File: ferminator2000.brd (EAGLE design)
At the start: 111.2 x 58 mm, 120 parts, among them CN1 MINIB, IC1 FT232RL, IC2 REF01D, Q1 STP5NA50, Q2 STP5NA50, SW1 ENCODER_SW1-PEC12, U1 DSPIC33FJ256GP510A

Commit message: added pin definitions
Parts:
- C1: value (none) -> 100u
- C14, C19, C20: value (none) -> 10u
- R10, R11, R12, R13, R8, R9: value 47k -> 10k
- R16: value 1k -> 22
- R2, R3: value 1K -> 1k
- R25, R26, R27, R28, R29, R30, R31, R32: value 1k -> 2.7k
- R4, R6: value 1k -> 5.6k
- R41, R42: value (none) -> 10k
- renumbered U$2 to U2

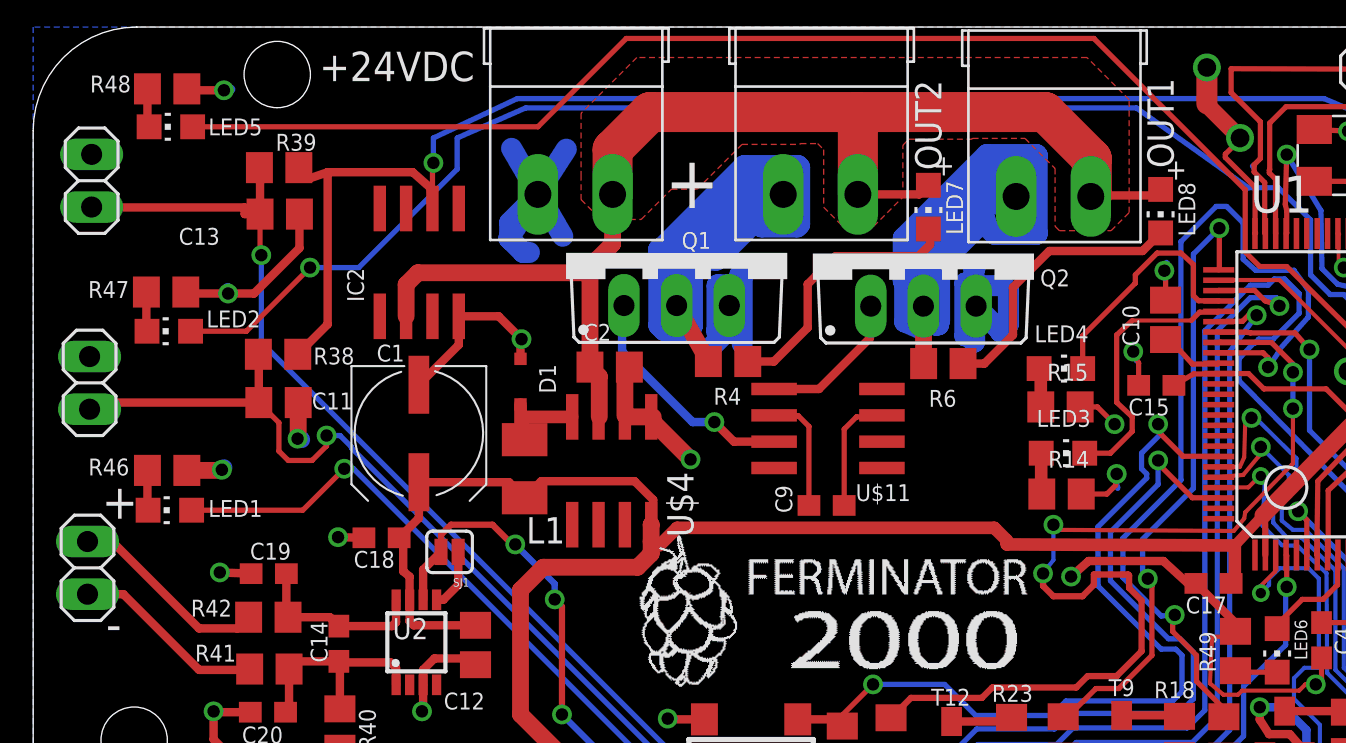
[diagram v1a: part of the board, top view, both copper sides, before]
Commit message: Added Control Lines for FETs
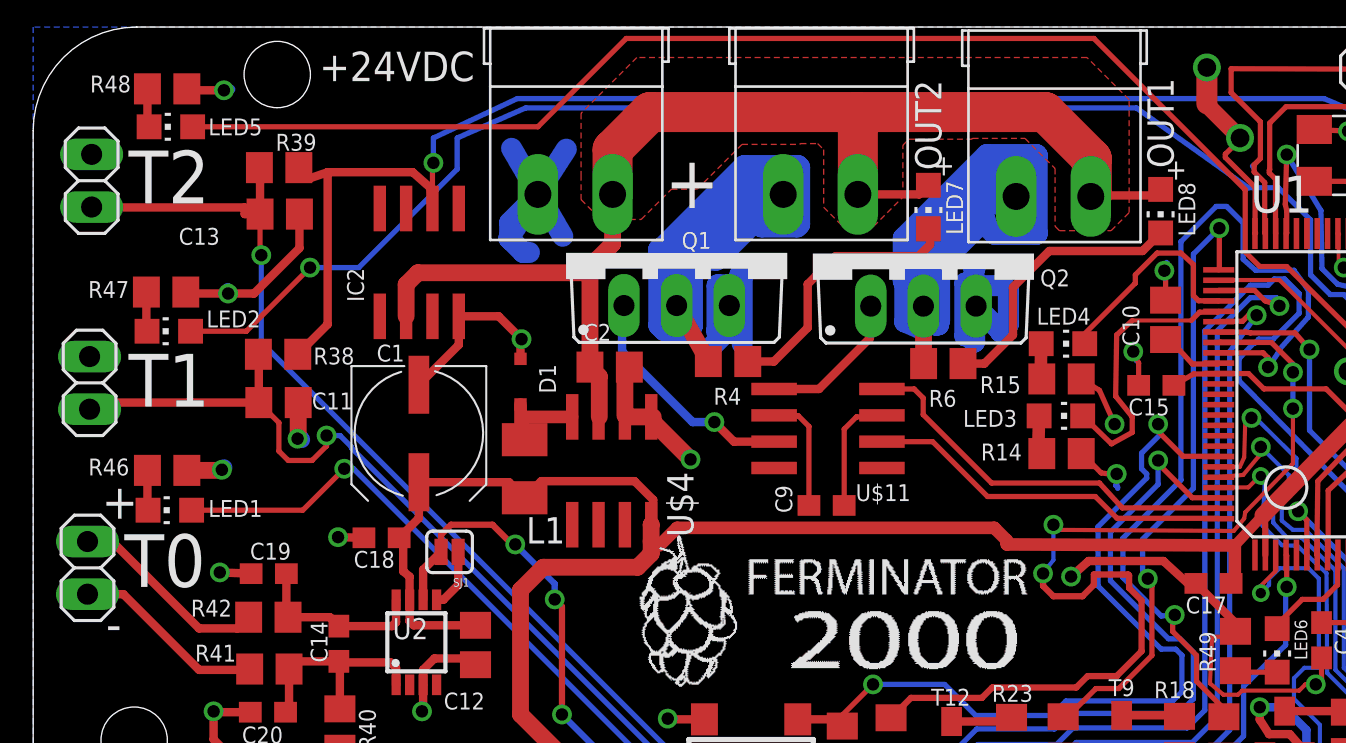
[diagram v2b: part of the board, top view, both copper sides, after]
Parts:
- moved R14 1.95 mm to (51.3, 38.0)
- moved LED3 1.80 mm to (51.2, 39.8)
- moved R15 1.35 mm to (51.3, 41.6)
- moved LED4 1.20 mm to (51.3, 43.3)
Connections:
- net HEATER1: now also U1.100
- net HEATER2: now also U1.99
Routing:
- net HEATER2: track 0.00 -> 19.1 mm
- net HEATER1: track 0.00 -> 17.8 mm
- net N$12: track 11.8 -> 10.7 mm
- net GND: track 209.3 -> 209.9 mm
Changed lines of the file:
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@@
 <layer number="43" name="vRestrict" color="2" fill="10" visible="no" active="yes"/>
 <layer number="44" name="Drills" color="7" fill="1" visible="no" active="yes"/>
-<layer number="45" name="Holes" color="7" fill="1" visible="yes" active="yes"/>
+<layer number="45" name="Holes" color="7" fill="1" visible="no" active="yes"/>
 <layer number="46" name="Milling" color="3" fill="1" visible="no" active="yes"/>
 <layer number="47" name="Measures" color="7" fill="1" visible="no" active="yes"/>
@@
 <layer number="144" name="Drill_legend" color="7" fill="1" visible="no" active="yes"/>
 <layer number="151" name="HeatSink" color="7" fill="1" visible="no" active="yes"/>
-<layer number="200" name="200bmp" color="1" fill="10" visible="yes" active="yes"/>
+<layer number="200" name="200bmp" color="1" fill="10" visible="no" active="yes"/>
 <layer number="201" name="201bmp" color="2" fill="10" visible="no" active="yes"/>
 <layer number="202" name="202bmp" color="3" fill="10" visible="no" active="yes"/>
@@
 <wire x1="107.68" y1="58.54" x2="6.68" y2="58.54" width="0" layer="20"/>
 <wire x1="6.68" y1="58.54" x2="1.68" y2="53.54" width="0" layer="20" curve="90"/>
-<text x="6.08" y="31.54" size="2.54" layer="51">T0</text>
-<text x="6.28" y="40.24" size="2.54" layer="51">T1</text>
-<text x="6.28" y="50.04" size="2.54" layer="51">T2</text>
+<text x="6.08" y="31.54" size="2.54" layer="25">T0</text>
+<text x="6.28" y="40.24" size="2.54" layer="25">T1</text>
+<text x="6.28" y="50.04" size="2.54" layer="25">T2</text>
 <text x="32.48" y="5.94" size="2.54" layer="51" rot="R90">SEL</text>
 <text x="32.78" y="17.64" size="2.54" layer="51" rot="R90">SET</text>
@@
 <attribute name="VALUE" x="71.655" y="51.995" size="1.27" layer="27" rot="R90"/>
 </element>
-<element name="LED3" library="led" package="CHIP-LED0805" value="" x="51.34" y="37.99" smashed="yes" rot="R270">
-<attribute name="NAME" x="50.07" y="39.26" size="0.8128" layer="25"/>
-<attribute name="VALUE" x="50.07" y="35.45" size="1.27" layer="27"/>
-</element>
-<element name="LED4" library="led" package="CHIP-LED0805" value="" x="51.24" y="42.07" smashed="yes" rot="R270">
-<attribute name="NAME" x="49.97" y="43.34" size="0.8128" layer="25"/>
-<attribute name="VALUE" x="49.97" y="39.53" size="1.27" layer="27"/>
-</element>
-<element name="R14" library="rcl" package="R0805" value="1k" x="51.27" y="36.02" smashed="yes">
-<attribute name="NAME" x="50.635" y="37.29" size="0.8128" layer="25"/>
-<attribute name="VALUE" x="50.635" y="33.48" size="1.27" layer="27"/>
-</element>
-<element name="R15" library="rcl" package="R0805" value="1k" x="51.22" y="40.22" smashed="yes">
-<attribute name="NAME" x="50.585" y="41.49" size="0.8128" layer="25"/>
-<attribute name="VALUE" x="50.585" y="37.68" size="1.27" layer="27"/>
+<element name="LED3" library="led" package="CHIP-LED0805" value="" x="51.24" y="39.79" smashed="yes" rot="R270">
+<attribute name="NAME" x="46.52" y="39.26" size="0.8128" layer="25"/>
+<attribute name="VALUE" x="49.97" y="37.25" size="1.27" layer="27"/>
+</element>
+<element name="LED4" library="led" package="CHIP-LED0805" value="" x="51.34" y="43.27" smashed="yes" rot="R270">
+<attribute name="NAME" x="50.07" y="44.19" size="0.8128" layer="25"/>
+<attribute name="VALUE" x="50.07" y="40.73" size="1.27" layer="27"/>
+</element>
+<element name="R14" library="rcl" package="R0805" value="1k" x="51.27" y="37.97" smashed="yes">
+<attribute name="NAME" x="47.385" y="37.64" size="0.8128" layer="25"/>
+<attribute name="VALUE" x="50.635" y="35.43" size="1.27" layer="27"/>
+</element>
+<element name="R15" library="rcl" package="R0805" value="1k" x="51.27" y="41.57" smashed="yes">
+<attribute name="NAME" x="47.335" y="40.89" size="0.8128" layer="25"/>
+<attribute name="VALUE" x="50.635" y="39.03" size="1.27" layer="27"/>
 </element>
 <element name="U1" library="main2" package="TQFP100" value="DSPIC33FJ256GP510A" x="66.6" y="40.83" smashed="yes">
@@
 <via x="10.78" y="37.19" extent="1-16" drill="0.6"/>
 <wire x1="10.78" y1="37.19" x2="10.88" y2="37.29" width="0.8128" layer="16"/>
-<wire x1="52.17" y1="40.22" x2="53" y2="40.22" width="0.254" layer="1"/>
-<wire x1="53" y1="40.22" x2="53.83" y2="39.39" width="0.254" layer="1"/>
+<wire x1="52.22" y1="41.57" x2="53.1" y2="41.02" width="0.254" layer="1"/>
+<wire x1="53.1" y1="41.02" x2="53.83" y2="39.39" width="0.254" layer="1"/>
 <via x="53.83" y="39.39" extent="1-16" drill="0.6"/>
 <wire x1="53.83" y1="39.39" x2="53.93" y2="39.29" width="0.254" layer="16"/>
@@
 <wire x1="78.33" y1="34.99" x2="78.28" y2="34.99" width="0.254" layer="16"/>
 <wire x1="63.42" y1="53.64" x2="63.46" y2="53.6" width="0.254" layer="1"/>
-<wire x1="52.22" y1="36.02" x2="53.46" y2="36.02" width="0.254" layer="1"/>
-<wire x1="53.46" y1="36.02" x2="53.88" y2="36.44" width="0.254" layer="1"/>
-<wire x1="53.88" y1="36.44" x2="53.88" y2="36.94" width="0.254" layer="1"/>
+<wire x1="52.22" y1="37.97" x2="52.36" y2="37.87" width="0.254" layer="1"/>
+<wire x1="52.36" y1="37.87" x2="53.18" y2="37.04" width="0.254" layer="1"/>
+<wire x1="53.18" y1="37.04" x2="53.88" y2="36.94" width="0.254" layer="1"/>
 <wire x1="53.88" y1="36.94" x2="53.93" y2="36.99" width="0.254" layer="1"/>
 <via x="53.93" y="36.99" extent="1-16" drill="0.6"/>
@@
 <contactref element="R14" pad="1"/>
 <contactref element="LED3" pad="A"/>
-<wire x1="50.29" y1="37.99" x2="50.29" y2="36.05" width="0.6096" layer="1"/>
-<wire x1="50.29" y1="36.05" x2="50.32" y2="36.02" width="0.6096" layer="1"/>
+<wire x1="50.19" y1="39.79" x2="50.14" y2="37.85" width="0.6096" layer="1"/>
+<wire x1="50.14" y1="37.85" x2="50.32" y2="37.97" width="0.6096" layer="1"/>
 </signal>
 <signal name="N$5">
 <contactref element="R15" pad="1"/>
 <contactref element="LED4" pad="A"/>
-<wire x1="50.27" y1="40.22" x2="50.27" y2="41.99" width="0.6096" layer="1"/>
-<wire x1="50.27" y1="41.99" x2="50.19" y2="42.07" width="0.6096" layer="1"/>
+<wire x1="50.32" y1="41.57" x2="50.27" y2="41.99" width="0.6096" layer="1"/>
+<wire x1="50.27" y1="41.99" x2="50.29" y2="43.27" width="0.6096" layer="1"/>
 </signal>
 <signal name="N$12">
 <contactref element="U1" pad="79"/>
 <contactref element="LED4" pad="C"/>
-<wire x1="52.29" y1="42.07" x2="52.29" y2="43.65" width="0.254" layer="1"/>
+<wire x1="52.39" y1="43.27" x2="52.29" y2="43.65" width="0.254" layer="1"/>
 <wire x1="52.29" y1="43.65" x2="54.83" y2="46.19" width="0.254" layer="1"/>
 <wire x1="54.83" y1="46.19" x2="54.83" y2="46.59" width="0.254" layer="1"/>
@@
 <contactref element="U1" pad="80"/>
 <contactref element="LED3" pad="C"/>
-<wire x1="52.39" y1="37.99" x2="53.63" y2="37.99" width="0.254" layer="1"/>
-<wire x1="53.63" y1="37.99" x2="54.68" y2="39.04" width="0.254" layer="1"/>
-<wire x1="54.68" y1="39.04" x2="54.68" y2="39.74" width="0.254" layer="1"/>
-<wire x1="54.68" y1="39.74" x2="53.93" y2="40.44" width="0.254" layer="1"/>
-<wire x1="53.93" y1="40.44" x2="53.93" y2="43.69" width="0.254" layer="1"/>
+<wire x1="52.29" y1="39.79" x2="53.68" y2="38.44" width="0.254" layer="1"/>
+<wire x1="53.68" y1="38.44" x2="54.68" y2="38.99" width="0.254" layer="1"/>
+<wire x1="54.68" y1="38.99" x2="54.68" y2="39.74" width="0.254" layer="1"/>
+<wire x1="54.68" y1="39.74" x2="53.88" y2="40.74" width="0.254" layer="1"/>
+<wire x1="53.88" y1="40.74" x2="53.93" y2="43.69" width="0.254" layer="1"/>
 <wire x1="53.93" y1="43.69" x2="54.68" y2="44.39" width="0.254" layer="1"/>
 <wire x1="54.68" y1="44.39" x2="57.53" y2="44.39" width="0.2" layer="1"/>
@@
 <signal name="HEATER1">
 <contactref element="U$11" pad="2"/>
+<contactref element="U1" pad="100"/>
+<wire x1="42.61" y1="38.545" x2="45.055" y2="38.545" width="0.254" layer="1"/>
+<wire x1="45.055" y1="38.545" x2="47.7" y2="35.9" width="0.254" layer="1"/>
+<wire x1="47.7" y1="35.9" x2="52.9" y2="35.9" width="0.254" layer="1"/>
+<wire x1="52.9" y1="35.9" x2="53.95" y2="34.85" width="0.254" layer="1"/>
+<wire x1="53.95" y1="34.85" x2="58.83" y2="34.85" width="0.254" layer="1"/>
+<wire x1="58.83" y1="34.85" x2="58.85" y2="34.83" width="0.254" layer="1"/>
 </signal>
 <signal name="HEATER2">
 <contactref element="U$11" pad="4"/>
+<contactref element="U1" pad="99"/>
+<wire x1="42.61" y1="41.085" x2="44.165" y2="41.085" width="0.254" layer="1"/>
+<wire x1="44.165" y1="41.085" x2="44.6" y2="40.65" width="0.254" layer="1"/>
+<wire x1="44.6" y1="40.65" x2="44.6" y2="39.85" width="0.254" layer="1"/>
+<wire x1="44.6" y1="39.85" x2="47.9" y2="36.55" width="0.254" layer="1"/>
+<wire x1="47.9" y1="36.55" x2="53.1" y2="36.55" width="0.254" layer="1"/>
+<wire x1="53.1" y1="36.55" x2="54.2" y2="35.35" width="0.254" layer="1"/>
+<wire x1="54.2" y1="35.35" x2="58.73" y2="35.35" width="0.254" layer="1"/>
+<wire x1="58.73" y1="35.35" x2="58.85" y2="35.33" width="0.254" layer="1"/>
 </signal>
 <signal name="N$22">

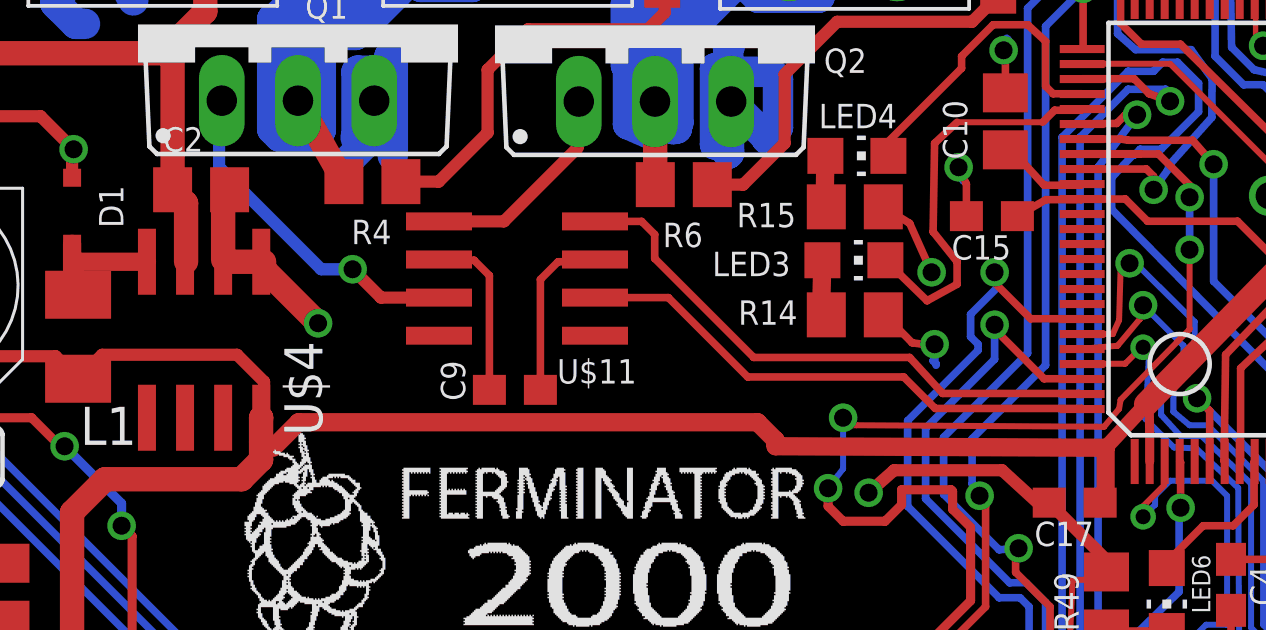
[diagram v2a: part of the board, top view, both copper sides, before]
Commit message: added power to TC4427
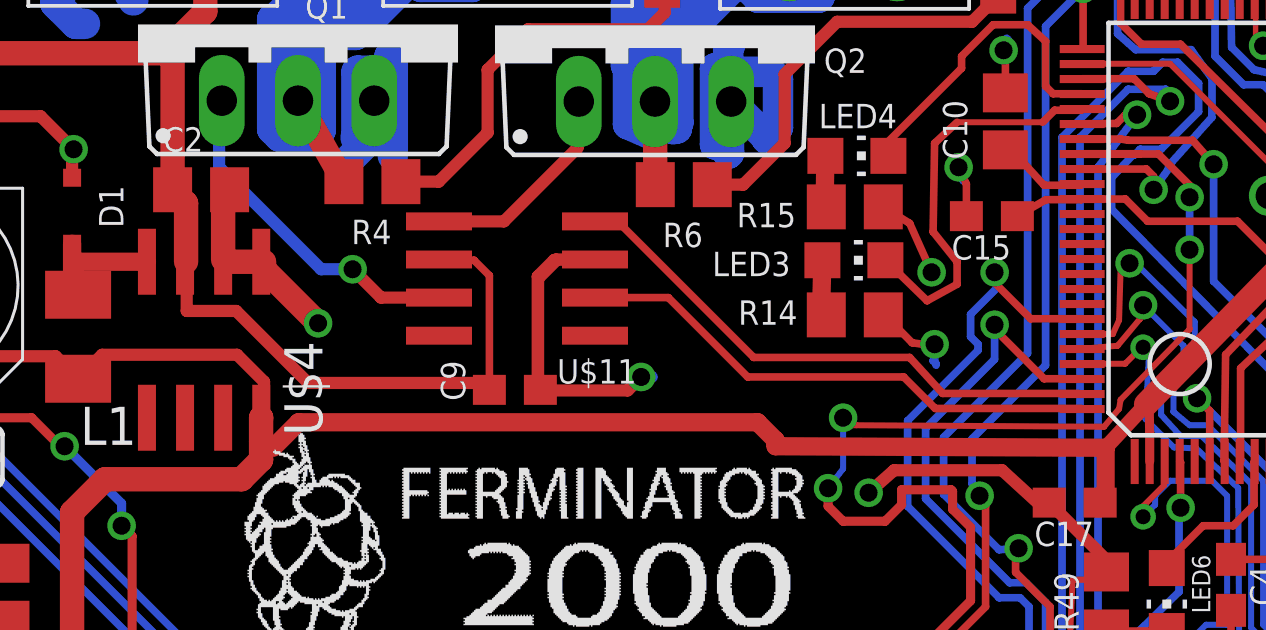
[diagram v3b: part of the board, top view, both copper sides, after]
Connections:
- removed net N$22: C9.1, U$11.6
- removed net N$23: C9.2, U$11.3
- net +24V: now also C9.1, U$11.6
- net GND: now also C9.2, U$11.3
- net HEATER1: now also U$11.4, U1.99; no longer U$11.2, U1.100
- net HEATER2: now also U$11.2, U1.100; no longer U$11.4, U1.99
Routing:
- net +24V: track 61.9 -> 80.4 mm
- net GND: track 209.9 -> 225.6 mm, vias 38 -> 39
- net N$23: track 5.78 -> 0.00 mm
- net N$22: track 5.71 -> 0.00 mm
- net HEATER2: track 19.1 -> 17.8 mm
- net HEATER1: track 17.8 -> 18.5 mm
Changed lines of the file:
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@@
 <wire x1="24.62" y1="48.36" x2="25.31" y2="47.67" width="1.016" layer="16"/>
 <wire x1="25.31" y1="47.67" x2="25.61" y2="47.67" width="1.016" layer="16"/>
+<contactref element="C9" pad="2"/>
+<contactref element="U$11" pad="3"/>
+<wire x1="40.79" y1="35.47" x2="40.79" y2="39.15" width="0.254" layer="1"/>
+<wire x1="40.79" y1="39.15" x2="41.38" y2="39.74" width="0.254" layer="1"/>
+<wire x1="41.38" y1="39.74" x2="42.535" y2="39.74" width="0.254" layer="1"/>
+<wire x1="42.535" y1="39.74" x2="42.61" y2="39.815" width="0.254" layer="1"/>
+<wire x1="42.61" y1="39.815" x2="41.315" y2="39.815" width="0.4064" layer="1"/>
+<wire x1="41.315" y1="39.815" x2="41.3" y2="39.8" width="0.4064" layer="1"/>
+<wire x1="41.3" y1="39.8" x2="41.25" y2="39.8" width="0.4064" layer="1"/>
+<wire x1="41.25" y1="39.8" x2="40.7" y2="39.25" width="0.4064" layer="1"/>
+<wire x1="40.7" y1="39.25" x2="40.7" y2="35.45" width="0.4064" layer="1"/>
+<wire x1="40.7" y1="35.45" x2="43.7" y2="35.45" width="0.4064" layer="1"/>
+<wire x1="43.7" y1="35.45" x2="44.15" y2="35.9" width="0.4064" layer="1"/>
+<via x="44.15" y="35.9" extent="1-16" drill="0.6"/>
+<wire x1="44.15" y1="35.9" x2="44.5" y2="35.9" width="0.4064" layer="16"/>
 </signal>
 <signal name="PGD1">
@@
 <vertex x="28.1" y="51.59"/>
 </polygon>
+<contactref element="C9" pad="1"/>
+<contactref element="U$11" pad="6"/>
+<wire x1="39.09" y1="35.47" x2="39.09" y2="39.28" width="0.254" layer="1"/>
+<wire x1="39.09" y1="39.28" x2="38.58" y2="39.79" width="0.254" layer="1"/>
+<wire x1="38.58" y1="39.79" x2="37.435" y2="39.79" width="0.254" layer="1"/>
+<wire x1="37.435" y1="39.79" x2="37.41" y2="39.815" width="0.254" layer="1"/>
+<wire x1="28.98" y1="39.74" x2="29" y2="39.74" width="0.4064" layer="1"/>
+<wire x1="29" y1="39.74" x2="29" y2="38.1" width="0.4064" layer="1"/>
+<wire x1="29" y1="38.1" x2="30.65" y2="38.1" width="0.4064" layer="1"/>
+<wire x1="30.65" y1="38.1" x2="33.05" y2="35.7" width="0.4064" layer="1"/>
+<wire x1="33.05" y1="35.7" x2="38.86" y2="35.7" width="0.4064" layer="1"/>
+<wire x1="38.86" y1="35.7" x2="39.09" y2="35.47" width="0.4064" layer="1"/>
 </signal>
 <signal name="+2.5VREF">
@@
 </signal>
 <signal name="HEATER1">
+<contactref element="U1" pad="99"/>
+<contactref element="U$11" pad="4"/>
+<wire x1="47.9" y1="36.55" x2="53.1" y2="36.55" width="0.254" layer="1"/>
+<wire x1="53.1" y1="36.55" x2="54.2" y2="35.35" width="0.254" layer="1"/>
+<wire x1="54.2" y1="35.35" x2="58.73" y2="35.35" width="0.254" layer="1"/>
+<wire x1="47.9" y1="36.55" x2="43.35" y2="41.1" width="0.254" layer="1"/>
+<wire x1="43.35" y1="41.1" x2="42.625" y2="41.1" width="0.254" layer="1"/>
+<wire x1="42.625" y1="41.1" x2="42.61" y2="41.085" width="0.254" layer="1"/>
+<wire x1="58.73" y1="35.35" x2="58.85" y2="35.33" width="0" layer="19" extent="1-1"/>
+</signal>
+<signal name="HEATER2">
+<contactref element="U1" pad="100"/>
 <contactref element="U$11" pad="2"/>
-<contactref element="U1" pad="100"/>
 <wire x1="42.61" y1="38.545" x2="45.055" y2="38.545" width="0.254" layer="1"/>
 <wire x1="45.055" y1="38.545" x2="47.7" y2="35.9" width="0.254" layer="1"/>
@@
 <wire x1="52.9" y1="35.9" x2="53.95" y2="34.85" width="0.254" layer="1"/>
 <wire x1="53.95" y1="34.85" x2="58.83" y2="34.85" width="0.254" layer="1"/>
-<wire x1="58.83" y1="34.85" x2="58.85" y2="34.83" width="0.254" layer="1"/>
-</signal>
-<signal name="HEATER2">
-<contactref element="U$11" pad="4"/>
-<contactref element="U1" pad="99"/>
-<wire x1="42.61" y1="41.085" x2="44.165" y2="41.085" width="0.254" layer="1"/>
-<wire x1="44.165" y1="41.085" x2="44.6" y2="40.65" width="0.254" layer="1"/>
-<wire x1="44.6" y1="40.65" x2="44.6" y2="39.85" width="0.254" layer="1"/>
-<wire x1="44.6" y1="39.85" x2="47.9" y2="36.55" width="0.254" layer="1"/>
-<wire x1="47.9" y1="36.55" x2="53.1" y2="36.55" width="0.254" layer="1"/>
-<wire x1="53.1" y1="36.55" x2="54.2" y2="35.35" width="0.254" layer="1"/>
-<wire x1="54.2" y1="35.35" x2="58.73" y2="35.35" width="0.254" layer="1"/>
-<wire x1="58.73" y1="35.35" x2="58.85" y2="35.33" width="0.254" layer="1"/>
-</signal>
-<signal name="N$22">
-<contactref element="C9" pad="1"/>
-<contactref element="U$11" pad="6"/>
-<wire x1="39.09" y1="35.47" x2="39.09" y2="39.28" width="0.254" layer="1"/>
-<wire x1="39.09" y1="39.28" x2="38.58" y2="39.79" width="0.254" layer="1"/>
-<wire x1="38.58" y1="39.79" x2="37.435" y2="39.79" width="0.254" layer="1"/>
-<wire x1="37.435" y1="39.79" x2="37.41" y2="39.815" width="0.254" layer="1"/>
-</signal>
-<signal name="N$23">
-<contactref element="C9" pad="2"/>
-<contactref element="U$11" pad="3"/>
-<wire x1="40.79" y1="35.47" x2="40.79" y2="39.15" width="0.254" layer="1"/>
-<wire x1="40.79" y1="39.15" x2="41.38" y2="39.74" width="0.254" layer="1"/>
-<wire x1="41.38" y1="39.74" x2="42.535" y2="39.74" width="0.254" layer="1"/>
-<wire x1="42.535" y1="39.74" x2="42.61" y2="39.815" width="0.254" layer="1"/>
+<wire x1="58.83" y1="34.85" x2="58.85" y2="34.83" width="0" layer="19" extent="1-1"/>
 </signal>
 <signal name="N$24">
